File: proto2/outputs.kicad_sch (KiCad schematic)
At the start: 72 parts, among them Q1 2N7002, Q10 2N7002, Q11 2N7002, Q12 2N7002, Q2 2N7002, Q3 2N7002, Q4 2N7002, Q5 2N7002, Q6 2N7002, Q7 2N7002, Q8 2N7002, Q9 2N7002, U1 AQY282SX, U10 AQY282SX, U11 AQY282SX, U12 AQY282SX, U2 AQY282SX, U3 AQY282SX, U4 AQY282SX, U5 AQY282SX, U6 AQY282SX, U7 AQY282SX, U8 AQY282SX, U9 AQY282SX

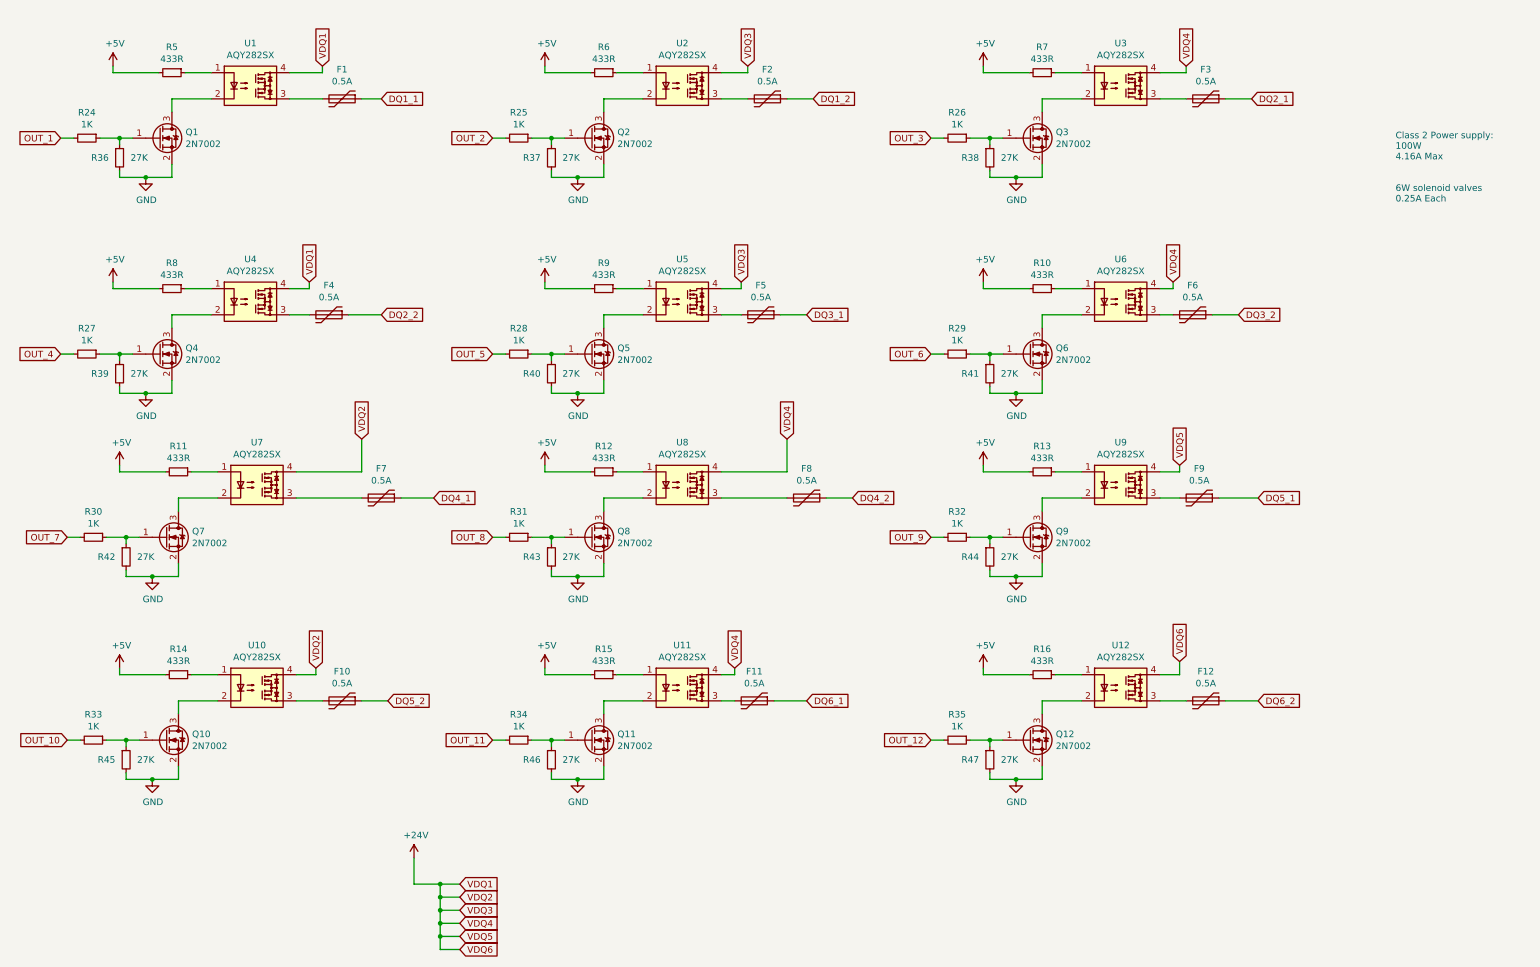
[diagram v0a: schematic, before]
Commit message: Added another 2 outputs and re-routed board.
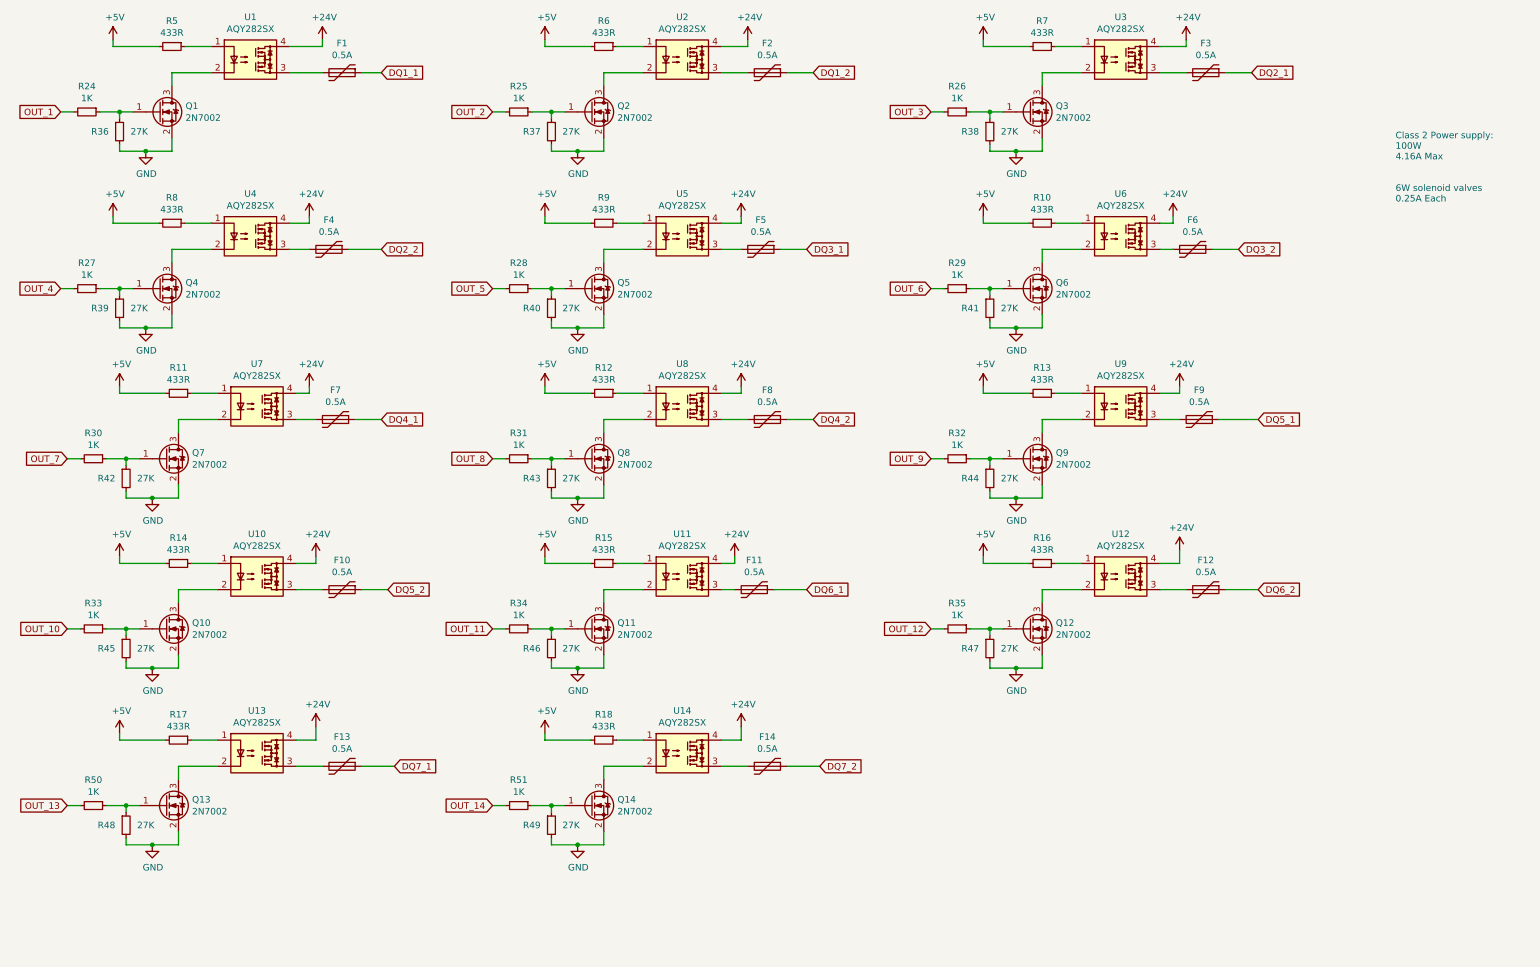
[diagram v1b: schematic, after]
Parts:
- added F13, F14: 0.5A, Resistor_SMD:R_1206_3216Metric, symbol Device:Polyfuse
- added Q13, Q14: 2N7002, Package_TO_SOT_SMD:SOT-23, symbol Transistor_FET:2N7002
- added R17, R18: 433R, Resistor_SMD:R_0805_2012Metric, symbol Device:R_Small
- added R48, R49: 27K, Resistor_SMD:R_0805_2012Metric, symbol Device:R_Small
- added R50, R51: 1K, Resistor_SMD:R_0805_2012Metric, symbol Device:R_Small
- added U13, U14: AQY282SX, Package_SO:SO-4_4.4x4.3mm_P2.54mm, symbol Relay_SolidState:ASSR-1218
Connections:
- net +24V: now also U13.4, U14.4
- net +5V: now also R17.2, R18.2
- net GND: now also Q13.2 (S), Q14.2 (S), R48.2, R49.2
- new net: R17.1, U13.1
- new net: Q13.3 (D), U13.2
- new net: F13.2, U13.3
- new net: Q14.1 (G), R49.1, R51.1
- new net: Q13.1 (G), R48.1, R50.1
- new net: R18.1, U14.1
- new net: Q14.3 (D), U14.2
- new net: F14.2, U14.3
- new net DQ7_1: F13.1
- new net DQ7_2: F14.1
- new net OUT_13: R50.2
- new net OUT_14: R51.2
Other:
- title: (none) -> Greenhouse 2.0 IO Board
- moved on the sheet: F1, F10, F11, F12, F2, F3, F4, F5, F6, F7, F8, F9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

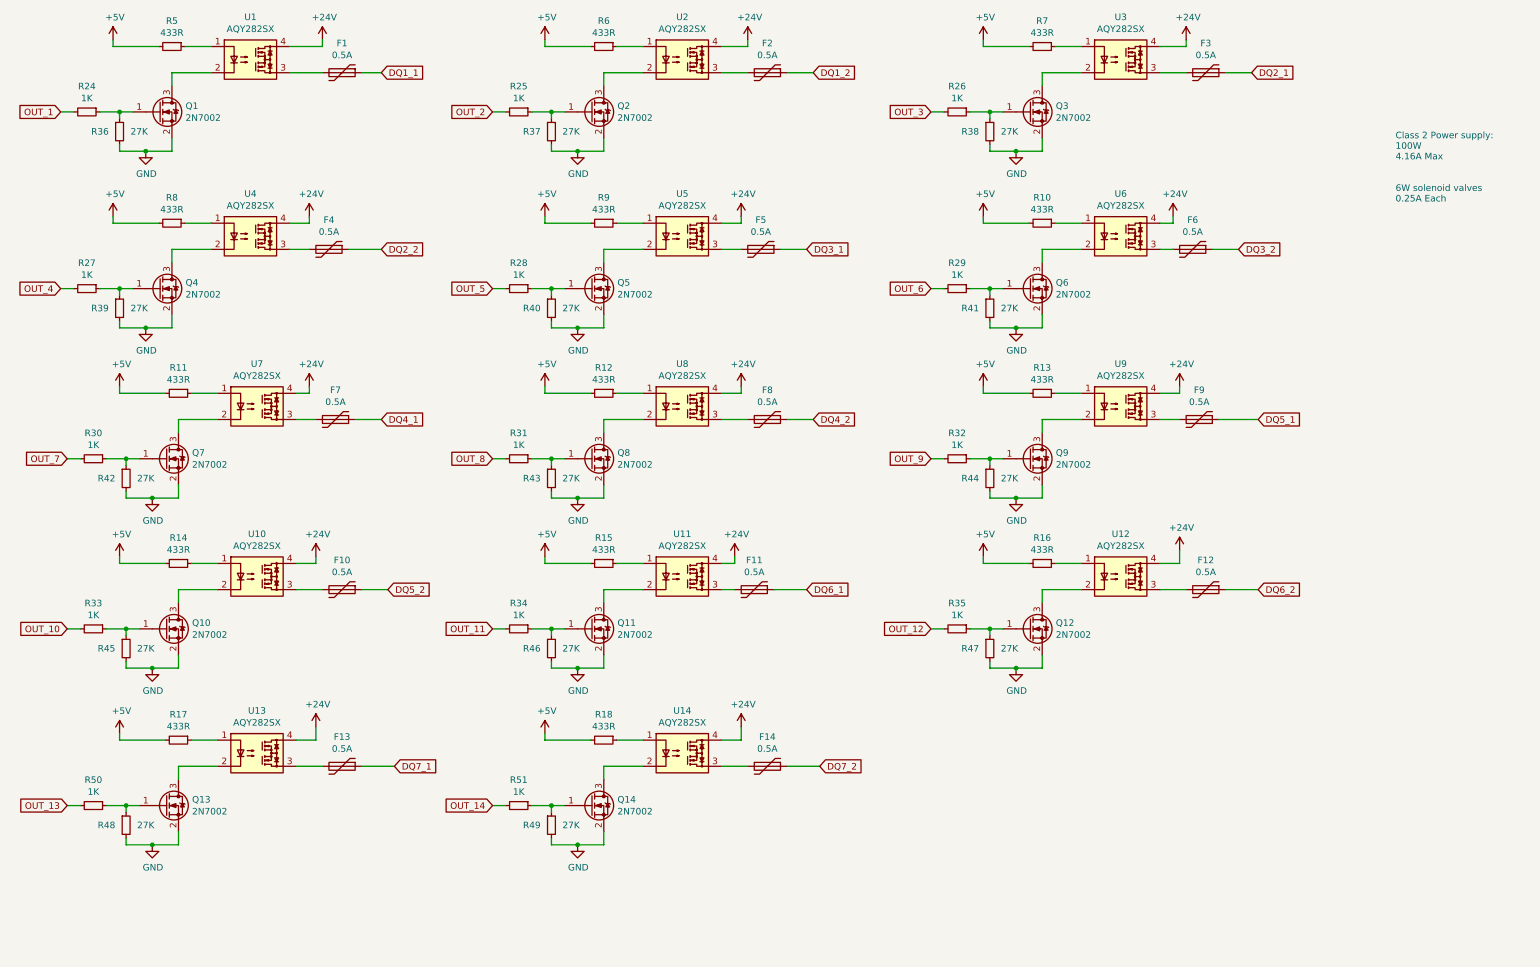
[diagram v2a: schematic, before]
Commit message: Laying out new filters and some schematic updates.
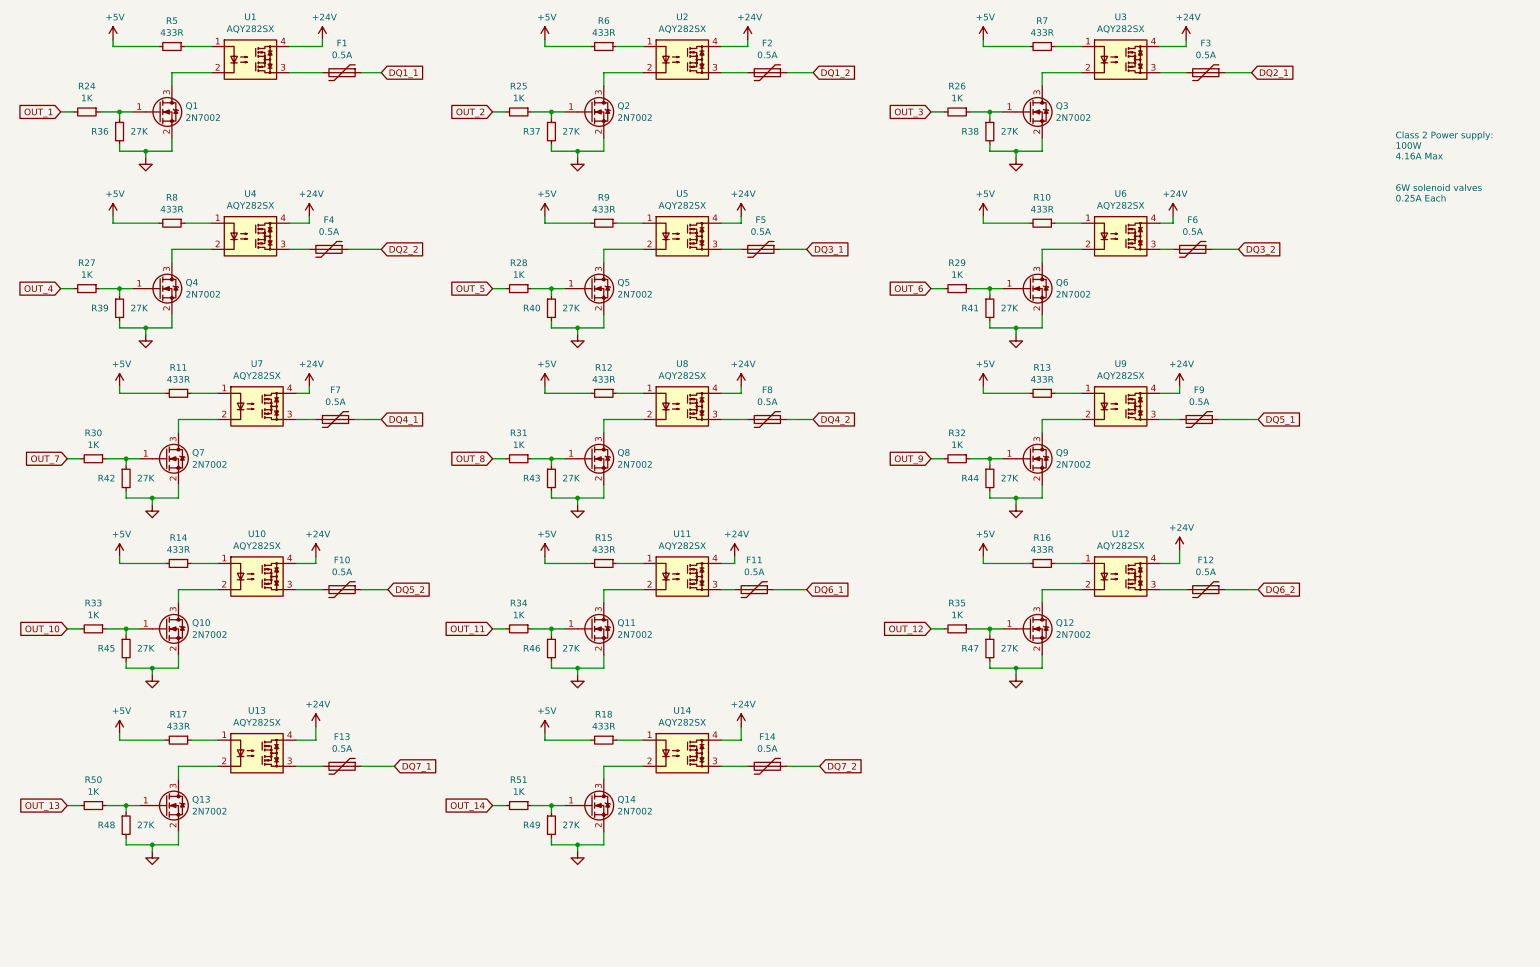
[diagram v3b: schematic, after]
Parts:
- Q1, Q10, Q11, Q12, Q13, Q14, Q2, Q3, Q4, Q5, Q6, Q7, Q8, Q9: LCSC (none) -> C8545
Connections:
- net GND renamed GND-SIG

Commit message: Fixed SSR footprint in schematic and corrected output pinout.
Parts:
- U1, U10, U11, U12, U13, U14, U2, U3, U4, U5, U6, U7, U8, U9: footprint Package_SO:SO-4_4.4x4.3mm_P2.54mm -> JLCPCB:SO-4_6.0mm_P2.54mm
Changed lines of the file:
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@@
   (title_block
     (title "Greenhouse 2.0 IO Board")
-    (date "2022-02-24")
+    (date "2022-03-06")
     (rev "0.2.0")
     (company "Langhe Greenhaus")
@@
     (property "Reference" "U1" (id 0) (at 60.96 14.605 0))
     (property "Value" "AQY282SX" (id 1) (at 60.96 16.9164 0))
-    (property "Footprint" "Package_SO:SO-4_4.4x4.3mm_P2.54mm" (id 2) (at 55.88 27.94 0)
+    (property "Footprint" "JLCPCB:SO-4_6.0mm_P2.54mm" (id 2) (at 55.88 27.94 0)
       (effects (font (size 1.27 1.27) italic) (justify left) hide)
     )
@@
     (property "Reference" "U4" (id 0) (at 60.96 48.895 0))
     (property "Value" "AQY282SX" (id 1) (at 60.96 51.2064 0))
-    (property "Footprint" "Package_SO:SO-4_4.4x4.3mm_P2.54mm" (id 2) (at 55.88 62.23 0)
+    (property "Footprint" "JLCPCB:SO-4_6.0mm_P2.54mm" (id 2) (at 55.88 62.23 0)
       (effects (font (size 1.27 1.27) italic) (justify left) hide)
     )
@@
     (property "Reference" "U7" (id 0) (at 62.23 81.915 0))
     (property "Value" "AQY282SX" (id 1) (at 62.23 84.2264 0))
-    (property "Footprint" "Package_SO:SO-4_4.4x4.3mm_P2.54mm" (id 2) (at 57.15 95.25 0)
+    (property "Footprint" "JLCPCB:SO-4_6.0mm_P2.54mm" (id 2) (at 57.15 95.25 0)
       (effects (font (size 1.27 1.27) italic) (justify left) hide)
     )
@@
     (property "Reference" "U10" (id 0) (at 62.23 114.935 0))
     (property "Value" "AQY282SX" (id 1) (at 62.23 117.2464 0))
-    (property "Footprint" "Package_SO:SO-4_4.4x4.3mm_P2.54mm" (id 2) (at 57.15 128.27 0)
+    (property "Footprint" "JLCPCB:SO-4_6.0mm_P2.54mm" (id 2) (at 57.15 128.27 0)
       (effects (font (size 1.27 1.27) italic) (justify left) hide)
     )
@@
     (property "Reference" "U2" (id 0) (at 144.78 14.605 0))
     (property "Value" "AQY282SX" (id 1) (at 144.78 16.9164 0))
-    (property "Footprint" "Package_SO:SO-4_4.4x4.3mm_P2.54mm" (id 2) (at 139.7 27.94 0)
+    (property "Footprint" "JLCPCB:SO-4_6.0mm_P2.54mm" (id 2) (at 139.7 27.94 0)
       (effects (font (size 1.27 1.27) italic) (justify left) hide)
     )
@@
     (property "Reference" "U5" (id 0) (at 144.78 48.895 0))
     (property "Value" "AQY282SX" (id 1) (at 144.78 51.2064 0))
-    (property "Footprint" "Package_SO:SO-4_4.4x4.3mm_P2.54mm" (id 2) (at 139.7 62.23 0)
+    (property "Footprint" "JLCPCB:SO-4_6.0mm_P2.54mm" (id 2) (at 139.7 62.23 0)
       (effects (font (size 1.27 1.27) italic) (justify left) hide)
     )
@@
     (property "Reference" "U8" (id 0) (at 144.78 81.915 0))
     (property "Value" "AQY282SX" (id 1) (at 144.78 84.2264 0))
-    (property "Footprint" "Package_SO:SO-4_4.4x4.3mm_P2.54mm" (id 2) (at 139.7 95.25 0)
+    (property "Footprint" "JLCPCB:SO-4_6.0mm_P2.54mm" (id 2) (at 139.7 95.25 0)
       (effects (font (size 1.27 1.27) italic) (justify left) hide)
     )
@@
     (property "Reference" "U11" (id 0) (at 144.78 114.935 0))
     (property "Value" "AQY282SX" (id 1) (at 144.78 117.2464 0))
-    (property "Footprint" "Package_SO:SO-4_4.4x4.3mm_P2.54mm" (id 2) (at 139.7 128.27 0)
+    (property "Footprint" "JLCPCB:SO-4_6.0mm_P2.54mm" (id 2) (at 139.7 128.27 0)
       (effects (font (size 1.27 1.27) italic) (justify left) hide)
     )
@@
     (property "Reference" "U3" (id 0) (at 229.87 14.605 0))
     (property "Value" "AQY282SX" (id 1) (at 229.87 16.9164 0))
-    (property "Footprint" "Package_SO:SO-4_4.4x4.3mm_P2.54mm" (id 2) (at 224.79 27.94 0)
+    (property "Footprint" "JLCPCB:SO-4_6.0mm_P2.54mm" (id 2) (at 224.79 27.94 0)
       (effects (font (size 1.27 1.27) italic) (justify left) hide)
     )
@@
     (property "Reference" "U6" (id 0) (at 229.87 48.895 0))
     (property "Value" "AQY282SX" (id 1) (at 229.87 51.2064 0))
-    (property "Footprint" "Package_SO:SO-4_4.4x4.3mm_P2.54mm" (id 2) (at 224.79 62.23 0)
+    (property "Footprint" "JLCPCB:SO-4_6.0mm_P2.54mm" (id 2) (at 224.79 62.23 0)
       (effects (font (size 1.27 1.27) italic) (justify left) hide)
     )
@@
     (property "Reference" "U9" (id 0) (at 229.87 81.915 0))
     (property "Value" "AQY282SX" (id 1) (at 229.87 84.2264 0))
-    (property "Footprint" "Package_SO:SO-4_4.4x4.3mm_P2.54mm" (id 2) (at 224.79 95.25 0)
+    (property "Footprint" "JLCPCB:SO-4_6.0mm_P2.54mm" (id 2) (at 224.79 95.25 0)
       (effects (font (size 1.27 1.27) italic) (justify left) hide)
     )
@@
     (property "Reference" "U12" (id 0) (at 229.87 114.935 0))
     (property "Value" "AQY282SX" (id 1) (at 229.87 117.2464 0))
-    (property "Footprint" "Package_SO:SO-4_4.4x4.3mm_P2.54mm" (id 2) (at 224.79 128.27 0)
+    (property "Footprint" "JLCPCB:SO-4_6.0mm_P2.54mm" (id 2) (at 224.79 128.27 0)
       (effects (font (size 1.27 1.27) italic) (justify left) hide)
     )
@@
     (property "Reference" "U13" (id 0) (at 62.23 149.225 0))
     (property "Value" "AQY282SX" (id 1) (at 62.23 151.5364 0))
-    (property "Footprint" "Package_SO:SO-4_4.4x4.3mm_P2.54mm" (id 2) (at 57.15 162.56 0)
+    (property "Footprint" "JLCPCB:SO-4_6.0mm_P2.54mm" (id 2) (at 57.15 162.56 0)
       (effects (font (size 1.27 1.27) italic) (justify left) hide)
     )
@@
     (property "Reference" "U14" (id 0) (at 144.78 149.225 0))
     (property "Value" "AQY282SX" (id 1) (at 144.78 151.5364 0))
-    (property "Footprint" "Package_SO:SO-4_4.4x4.3mm_P2.54mm" (id 2) (at 139.7 162.56 0)
+    (property "Footprint" "JLCPCB:SO-4_6.0mm_P2.54mm" (id 2) (at 139.7 162.56 0)
       (effects (font (size 1.27 1.27) italic) (justify left) hide)
     )
